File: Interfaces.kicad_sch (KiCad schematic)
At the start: 10 parts, among them J10 200528-0100, J7 1824543, J8 Conn_01x06

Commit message: Changes for lib refactor
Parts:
- J7: footprint Battery-Board:1824543 -> Argus-Connectors:1824543; symbol Battery-Board:1824543 -> Argus-Connectors:1824543
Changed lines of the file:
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@@
 	)
 	(symbol
-		(lib_id "Battery-Board:1824543")
+		(lib_id "Argus-Connectors:1824543")
 		(at 80.01 83.82 0)
 		(unit 1)
@@
 			)
 		)
-		(property "Footprint" "Battery-Board:1824543"
+		(property "Footprint" "Argus-Connectors:1824543"
 			(at 96.52 178.74 0)
 			(effects

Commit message: Fixes from feedback
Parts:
- J7: footprint Argus-Connectors:1824543 -> 1824543
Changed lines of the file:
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@@
 			)
 		)
-		(property "Footprint" "Argus-Connectors:1824543"
+		(property "Footprint" "1824543"
 			(at 96.52 178.74 0)
 			(effects

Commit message: v2.1 (v3?) Partial Updates
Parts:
- removed C17: 10uF, Capacitor_SMD:C_0805_2012Metric, symbol Device:C_Small
- removed D1: 4.7V, Diode_SMD:D_SMA, symbol Device:D_Zener_Small
- removed F1: 1A, Fuse:Fuse_0805_2012Metric, symbol Device:Polyfuse
- removed J7: 1824543, 1824543, symbol Argus-Connectors:1824543
- removed J8: Conn_01x06, Connector_PinHeader_2.54mm:PinHeader_1x06_P2.54mm_Vertical, symbol Connector_Generic:Conn_01x06
- added C19: 10uF, Capacitor_SMD:C_0805_2012Metric, symbol Device:C_Small
- added D6: 4.7V, Diode_SMD:D_SMA, symbol Device:D_Zener_Small
- added J6: Conn_01x04, symbol Connector_Generic:Conn_01x04
- D7: renamed from D5; symbol Device:D_Schottky_Dual_Series_ACK -> Device:D_Schottky_Dual_Series_AKC
- D8: renamed from D4; symbol Device:D_Schottky_Dual_Series_ACK -> Device:D_Schottky_Dual_Series_AKC
- D9: renamed from D3; symbol Device:D_Schottky_Dual_Series_ACK -> Device:D_Schottky_Dual_Series_AKC
- renumbered D2 to D5, J10 to J7
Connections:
- net +3V3_PS is gone; now on net +3V3: J7.10 (Pin_10), J7.9 (Pin_9)
- net +3V3: now also D7.2 (K), D8.2 (K), D9.2 (K), C19.1, D6.1 (K); no longer D7.3 (K), D8.3 (K), D9.3 (K)
- net ALERT: now also D9.3 (common); no longer D9.2 (common)
- net GND: now also C19.2, D6.2 (A)
- net SCL_BUS: now also D8.3 (common); no longer D8.2 (common)
- net SDA_BUS: now also D7.3 (common); no longer D7.2 (common)
- net SYSTEM_VDD: now also J6.1 (Pin_1), J6.3 (Pin_3)
- net SYSTEM_VSS: now also J6.2 (Pin_2), J6.4 (Pin_4)
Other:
- note added: "USE SMALLER FOOTPRINT"
- company: (none) -> Carnegie Mellon University
- title: (none) -> Argus Batteryboard
- moved on the sheet: D5, D8, D9, J7

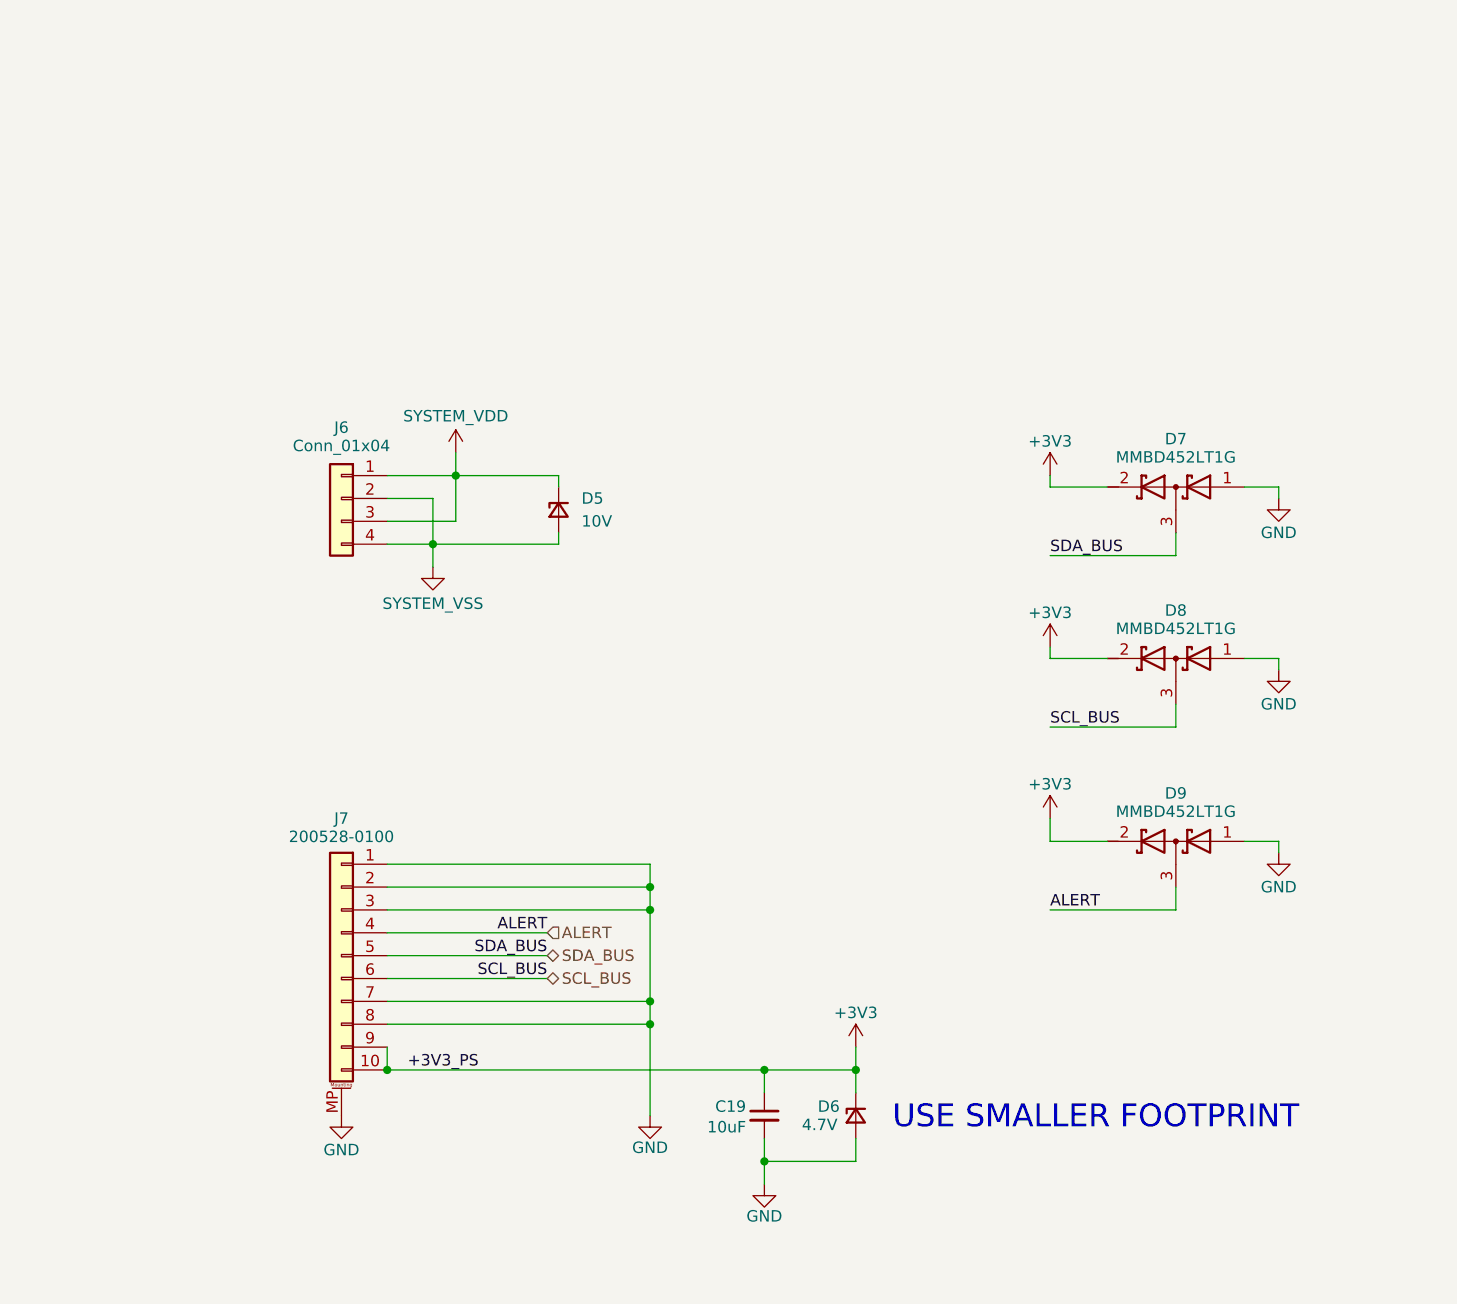
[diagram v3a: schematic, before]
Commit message: Silkscreen cleanup
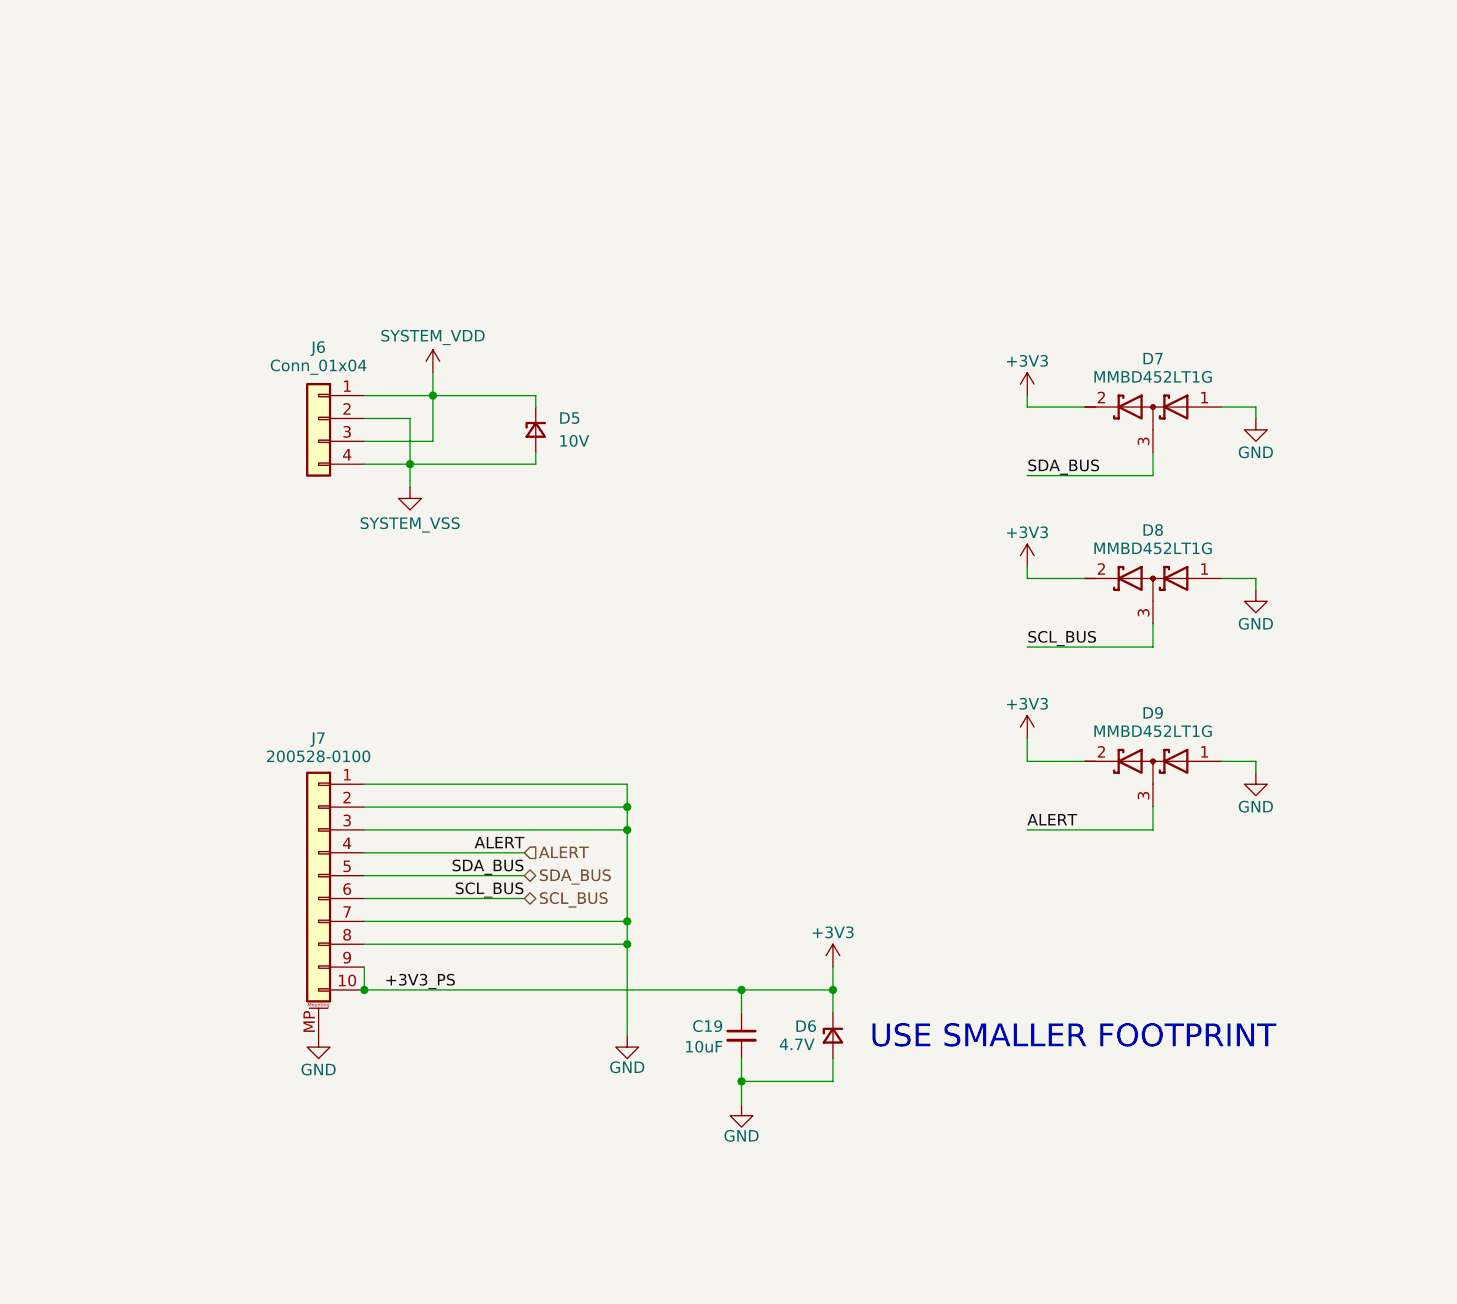
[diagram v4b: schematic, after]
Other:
- moved on the sheet: C19, D5, D6, D7, D8, D9, J6, J7

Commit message: More updates
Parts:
- removed D6: 4.7V, Diode_SMD:D_SMA, symbol Device:D_Zener_Small
- removed D7, D8, D9: MMBD452LT1G, Package_TO_SOT_SMD:SOT-23-3, symbol Device:D_Schottky_Dual_Series_AKC
- added J8: IO Header, Connector_PinHeader_2.54mm:PinHeader_1x05_P2.54mm_Vertical_SMD_Pin1Left, symbol Connector_Generic:Conn_01x05
- added U3, U7: D5V0P4UR6SO, Package_TO_SOT_SMD:SOT-23-6, symbol Power_Protection:SRV05-4
- D5: Part (none) -> SMAJ9.0AHR3G
- J6: value Conn_01x04 -> 282834-4; footprint (none) -> TerminalBlock_TE-Connectivity:TerminalBlock_TE_282834-4_1x04_P2.54mm_Horizontal
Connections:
- net +3V3: now also J8.1 (Pin_1), U3.5 (VP), U7.5 (VP)
- net ALERT: now also J8.5 (Pin_5), U3.4 (IO3)
- net GND: now also J8.2 (Pin_2), U3.2 (VN), U7.2 (VN); no longer J7.1 (Pin_1), J7.2 (Pin_2), J7.3 (Pin_3)
- net SCL_BUS: now also J8.3 (Pin_3), U7.3 (IO2)
- net SDA_BUS: now also J8.4 (Pin_4), U7.1 (IO1)
- new net HEAT0_ON: J7.3 (Pin_3), U3.3 (IO2)
- new net HEAT1_ON: J7.2 (Pin_2), U3.1 (IO1)
- new net HEATER_ENABLE: J7.1 (Pin_1), U3.6 (IO4)
- no-connect marks 0 -> 2
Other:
- note added: "FPC to Mainboard"
- note added: "Power Connector"
- note removed: "USE SMALLER FOOTPRINT"
- moved on the sheet: C19, D5, J6, J7

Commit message: Finalized updates with recommendations and exported files
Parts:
- removed J8: IO Header, Connector_PinHeader_2.54mm:PinHeader_1x05_P2.54mm_Vertical_SMD_Pin1Left, symbol Connector_Generic:Conn_01x05
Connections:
- net HEAT0_ON renamed HEATER0_ON
- net HEAT1_ON renamed HEATER1_ON

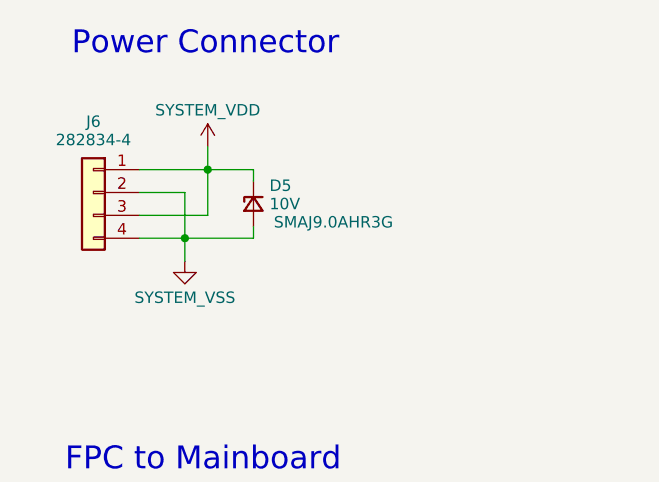
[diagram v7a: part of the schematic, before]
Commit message: Updated board outline and power pinout
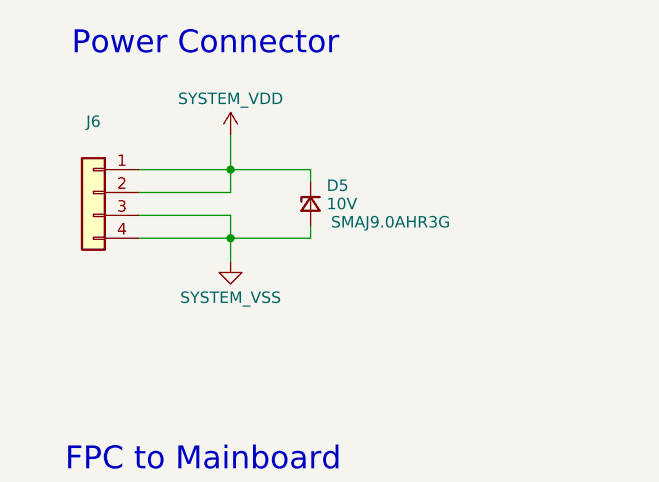
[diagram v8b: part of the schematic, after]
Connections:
- net SYSTEM_VDD: now also J6.2 (Pin_2); no longer J6.3 (Pin_3)
- net SYSTEM_VSS: now also J6.3 (Pin_3); no longer J6.2 (Pin_2)
